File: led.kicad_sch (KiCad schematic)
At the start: 4 parts, among them Q1 MMBT3904

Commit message: Added LSCS part numbers to all components
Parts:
- D1: LCSC (none) -> C2286
- Q1: LCSC (none) -> C7420353
- R1: LCSC (none) -> C25890
- R2: LCSC (none) -> C25076
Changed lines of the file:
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@@
+			)
+		)
+		(property "LCSC" "C25890"
+			(at 139.7 88.9 90)
+			(effects
+				(font
+					(size 1.27 1.27)
+				)
+				(hide yes)
 			)
 		)
@@
 		)
 		(property "Description" "Resistor"
+			(at 152.4 78.74 0)
+			(effects
+				(font
+					(size 1.27 1.27)
+				)
+				(hide yes)
+			)
+		)
+		(property "LCSC" "C25076"
 			(at 152.4 78.74 0)
 			(effects
@@
 			)
 		)
+		(property "LCSC" "C7420353"
+			(at 149.86 88.9 0)
+			(effects
+				(font
+					(size 1.27 1.27)
+				)
+				(hide yes)
+			)
+		)
 		(pin "1"
 		)
@@
 			(effects
 				(font
+					(size 1.27 1.27)
+				)
+				(hide yes)
+			)
+		)
+		(property "LCSC" "C2286"
+			(at 152.4 71.12 90)
+			(effects
+				(font

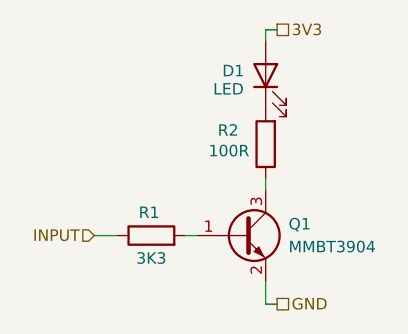
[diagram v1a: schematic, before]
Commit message: Improved layout to remove symbol warnings
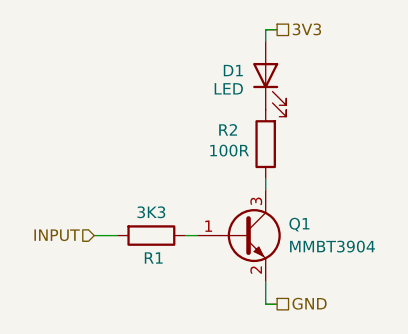
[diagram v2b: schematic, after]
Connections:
- net INPUT: now also R1.2; no longer R1.1
- net at Q1.1 (B): now also R1.1; no longer R1.2
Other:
- moved on the sheet: R1
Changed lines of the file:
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@@
 	(symbol
 		(lib_id "Device:R")
-		(at 139.7 88.9 90)
+		(at 139.7 88.9 270)
 		(unit 1)
 		(exclude_from_sim no)
@@
 		(dnp no)
 		(property "Reference" "R1"
-			(at 139.446 86.36 90)
+			(at 139.954 91.44 90)
 			(effects
 				(font
@@
 		)
 		(property "Value" "3K3"
-			(at 139.7 91.44 90)
+			(at 139.7 86.36 90)
 			(effects
 				(font
@@
 		)
 		(property "Footprint" "Resistor_SMD:R_0402_1005Metric"
-			(at 139.7 90.678 90)
+			(at 139.7 87.122 90)
 			(effects
 				(font
